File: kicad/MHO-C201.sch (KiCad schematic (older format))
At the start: 7 parts, among them P1 Conn_01x10_Female

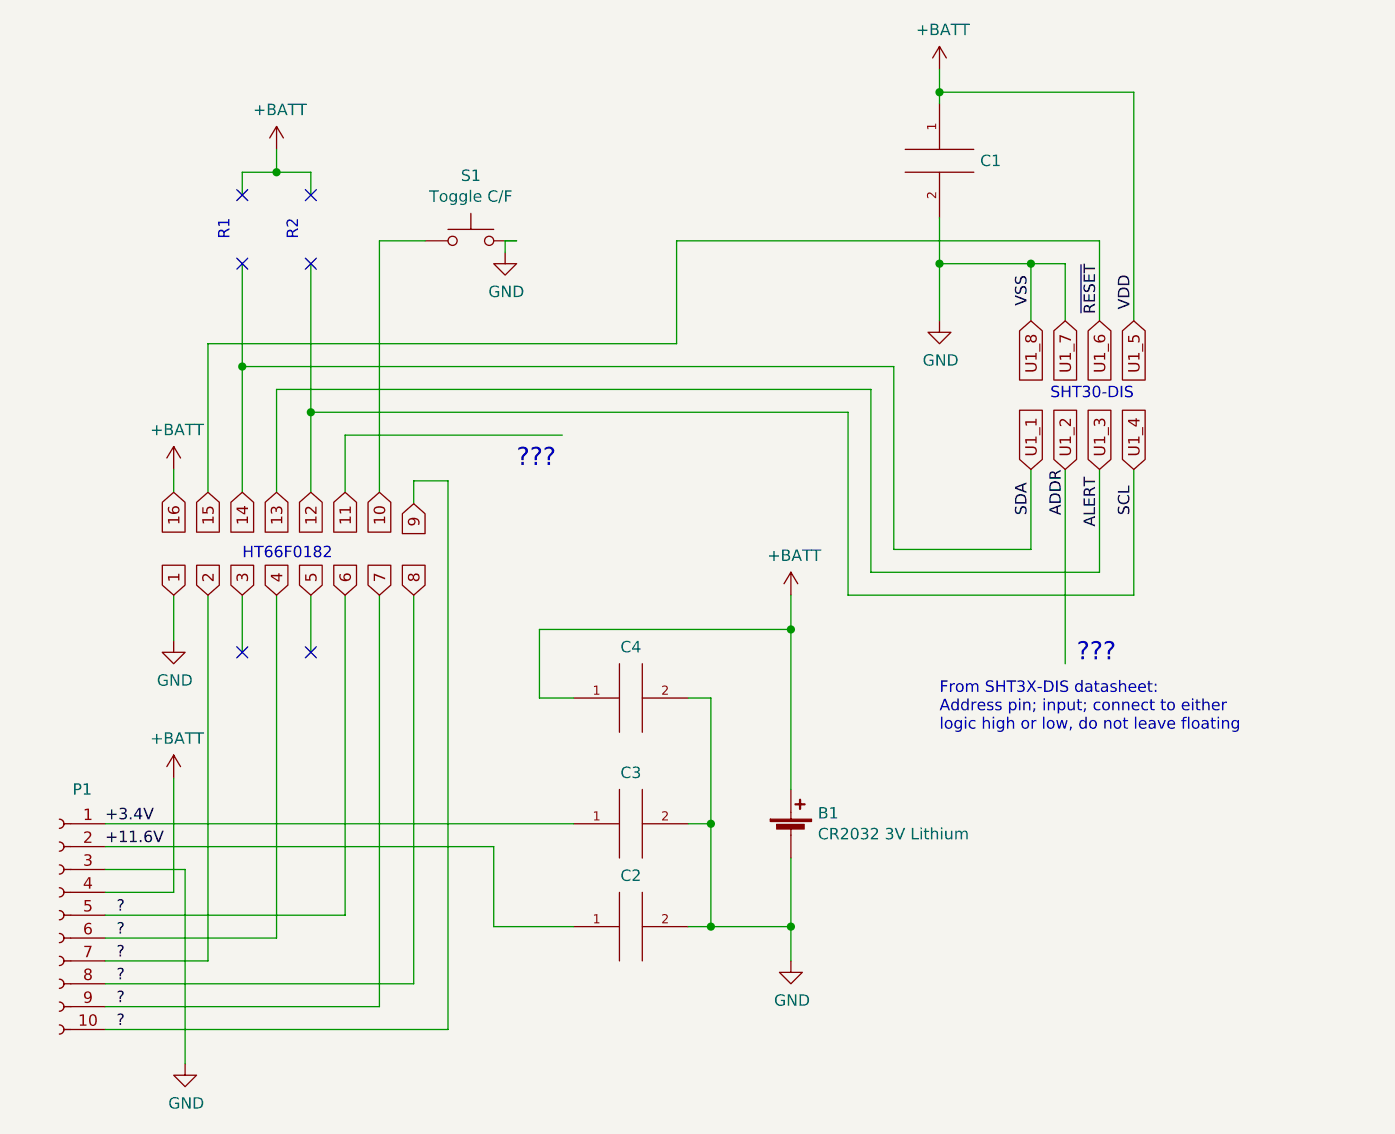
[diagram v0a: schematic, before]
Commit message: Update schematic so it's more compact
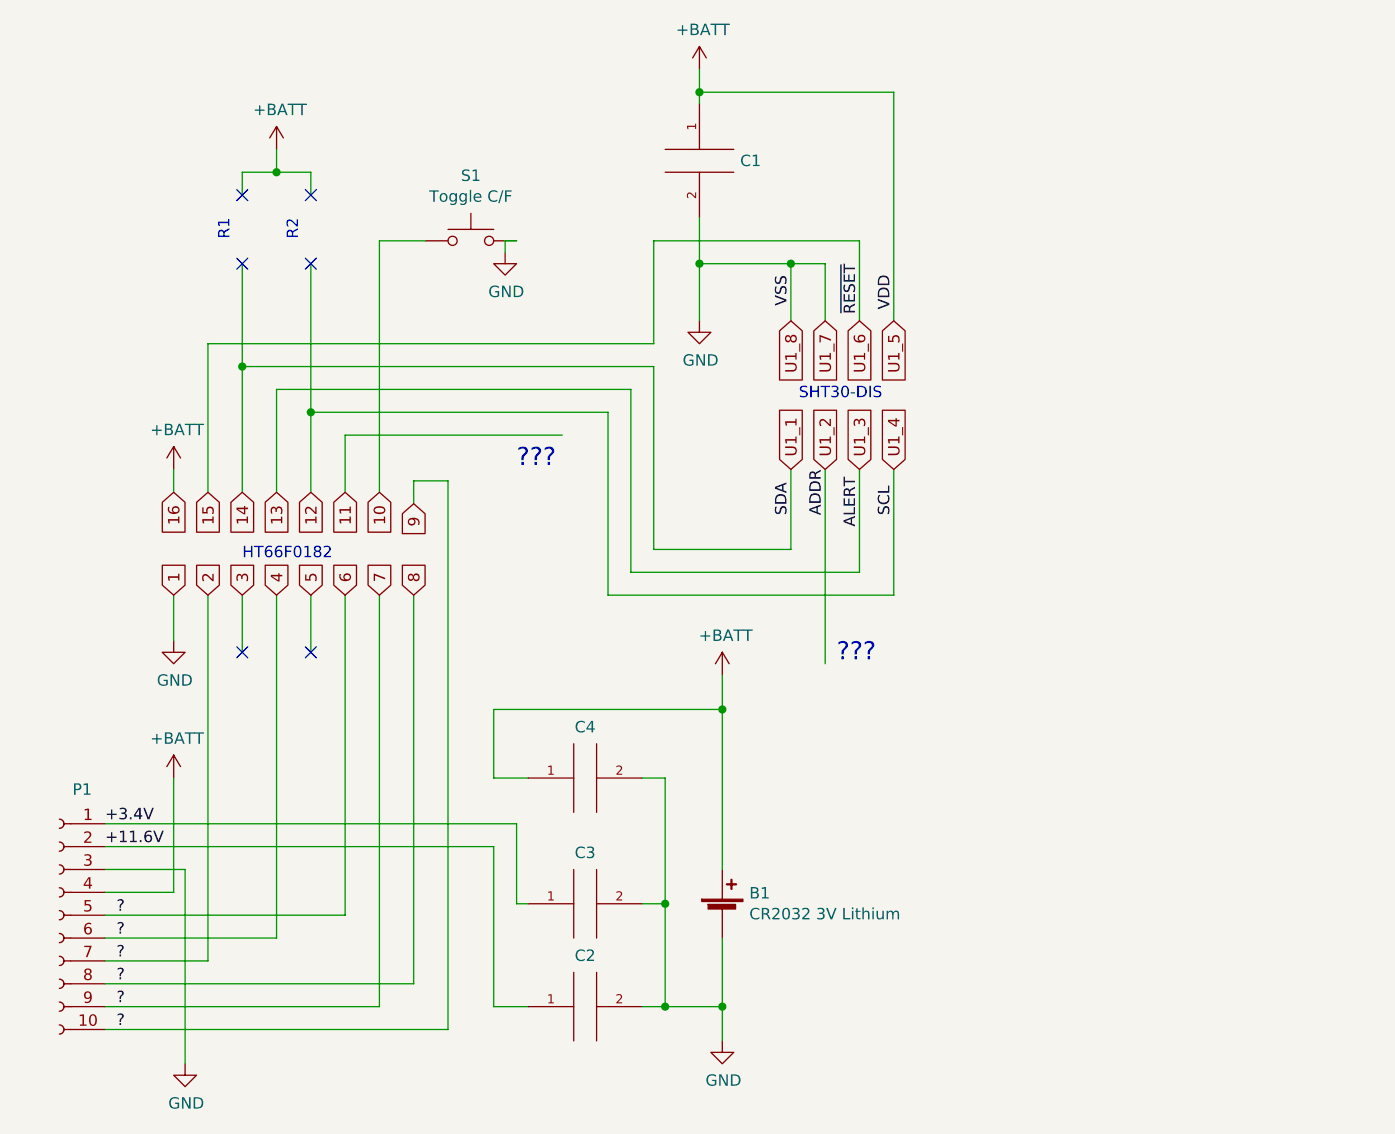
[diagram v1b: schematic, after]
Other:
- note removed: "From SHT3X-DIS datasheet:\nAddress pin; input; connect to either\nlogic high or low, do not leave floating"
- moved on the sheet: B1, C1, C2, C3, C4

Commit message: Add notes about the display update process
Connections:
- net 12: now also P1.8 (Pin_8)
- net 14: now also P1.7 (Pin_7)
- net +11.6V renamed VHL+11.6V
- net +3.4V renamed VDL+3.4V
- removed net 2: P1.10 (Pin_10), P1.5 (Pin_5), P1.6 (Pin_6), P1.7 (Pin_7), P1.8 (Pin_8), P1.9 (Pin_9)
- new net 4: P1.6 (Pin_6)
- new net 6: P1.5 (Pin_5)
- new net 7: P1.9 (Pin_9)
- new net 9: P1.10 (Pin_10)
- no-connect marks 6 -> 8
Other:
- note added: "HT16E07 (probably)"
- note removed: "???"
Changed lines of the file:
@@
 SCL
 Wire Wire Line
-	4550 2700 4550 3550
+	4550 2700 4550 3050
 Text Label 4550 2900 1    50   ~ 0
 ADDR
@@
 	2450 2800 2450 2550
 Wire Wire Line
-	2450 2550 3400 2550
-Wire Wire Line
 	2150 2800 2150 2350
 Wire Wire Line
@@
 	2300 3250 2300 3500
 NoConn ~ 2300 3500
-Text Notes 3200 2700 0    79   ~ 0
-???
-Text Notes 4600 3550 0    79   ~ 0
-???
 NoConn ~ 2000 1800
 NoConn ~ 2300 1800
@@
 	2300 2450 2300 2800
 Text Label 1400 4350 0    50   ~ 0
-+11.6V
+VHL+11.6V
 Text Label 1400 4250 0    50   ~ 0
-+3.4V
-Text Label 1450 4650 0    50   ~ 0
-?
-Text Label 1450 4750 0    50   ~ 0
-?
-Text Label 1450 4850 0    50   ~ 0
-?
-Text Label 1450 4950 0    50   ~ 0
-?
-Text Label 1450 5050 0    50   ~ 0
-?
-Text Label 1450 5150 0    50   ~ 0
-?
+VDL+3.4V
+Text Label 1400 4650 0    50   ~ 0
+SHD_N
+Text Label 1400 4750 0    50   ~ 0
+RST_N
+Text Label 1400 4850 0    50   ~ 0
+SDA
+Text Label 1400 4950 0    50   ~ 0
+SCL
+Text Label 1400 5050 0    50   ~ 0
+CSB
+Text Label 1400 5150 0    50   ~ 0
+BUSY_N
 Text Notes 1950 1700 1    50   ~ 0
 R1
@@
 Wire Wire Line
 	3200 4600 3250 4600
+Text Label 1400 4450 0    50   ~ 0
+GND
+Text Label 1400 4550 0    50   ~ 0
+VIN
+Text Notes 1100 5050 1    50   ~ 0
+HT16E07 (probably)
+NoConn ~ 2450 2550
+NoConn ~ 4550 3050
 $EndSCHEMATC
